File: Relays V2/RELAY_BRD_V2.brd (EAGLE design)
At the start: 43.9 x 48 mm, 20 parts, among them Q1 MMBT2222A, U1 ACS712-30A

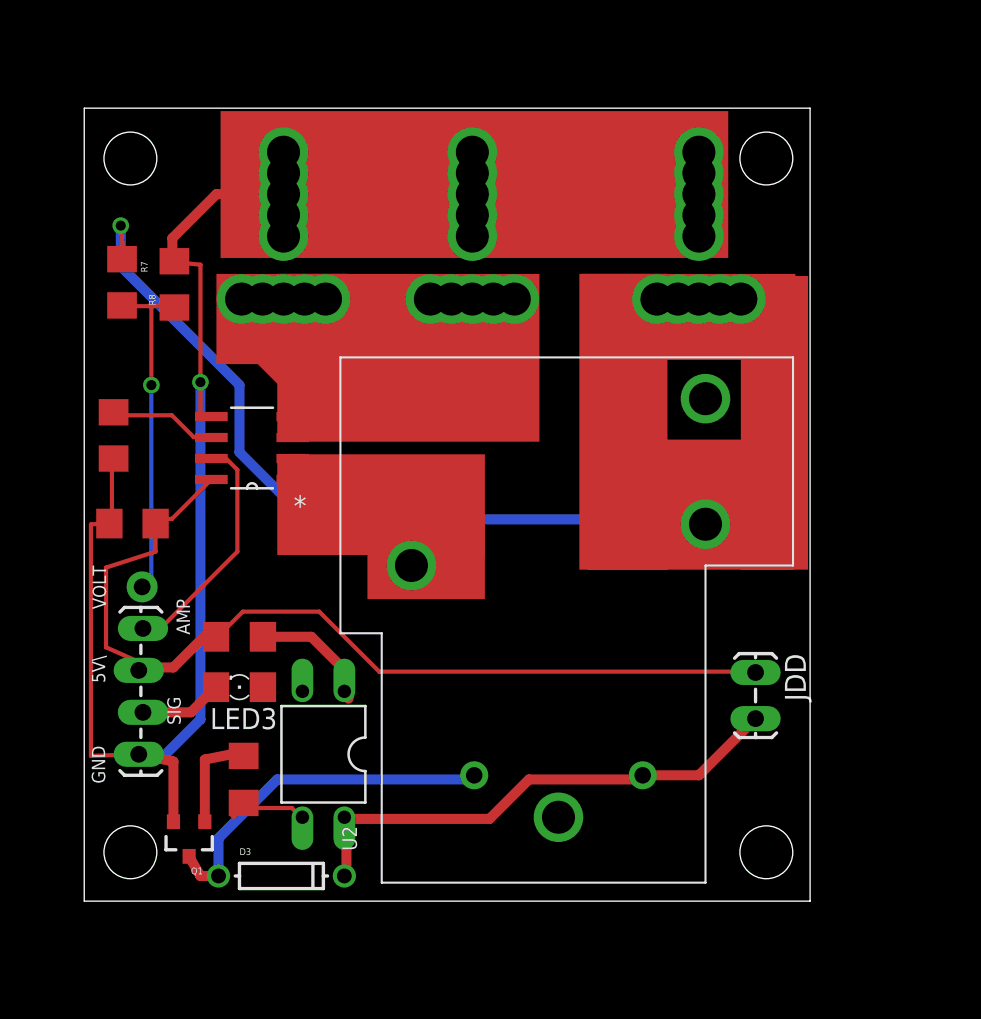
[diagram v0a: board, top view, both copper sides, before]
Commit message: added relays v2
added the new relays we will be using this year for robosub
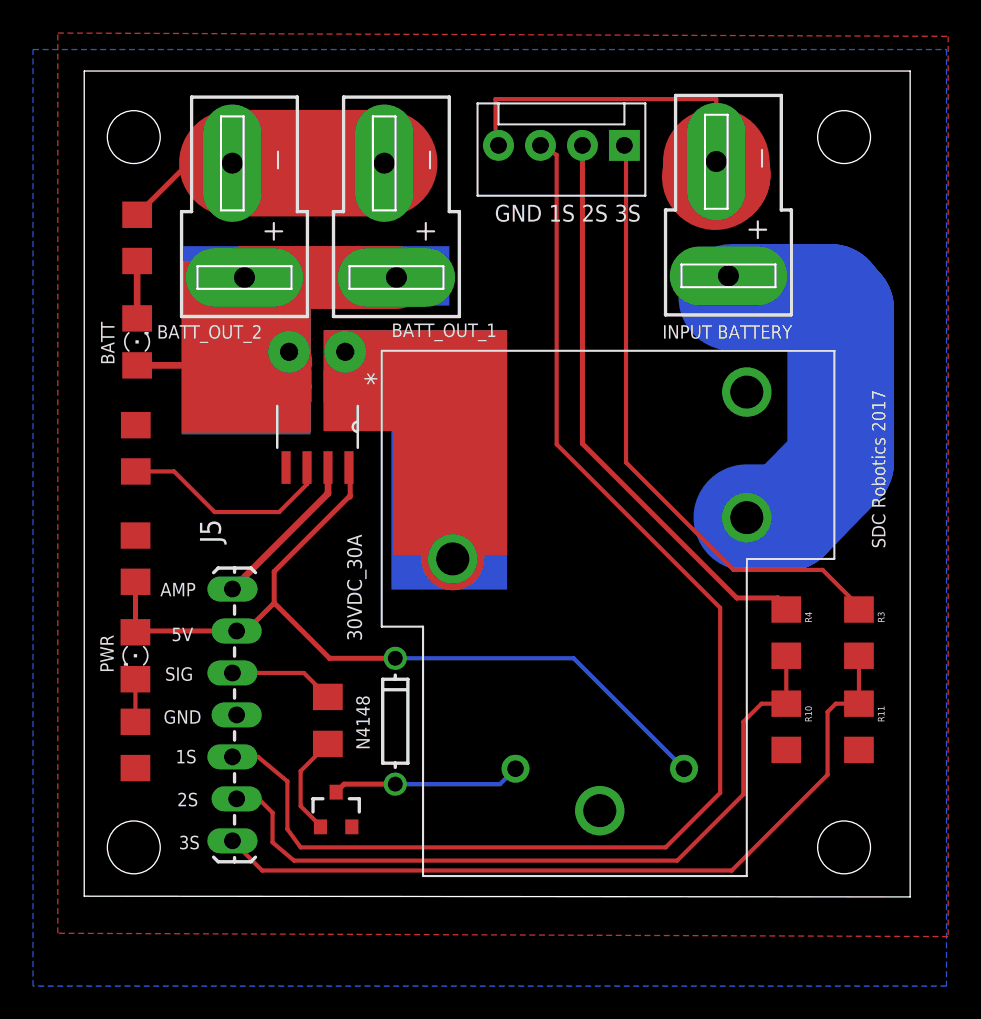
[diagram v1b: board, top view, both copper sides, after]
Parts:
- removed 11.1V_DEAN_CONNECTOR, J2, J6, J7: (no value), SparkFun-Connectors:1X01NS-KIT
- removed J9: (no value), SparkFun-Connectors:1X04_LOCK_LONGPADS
- removed JDD: (no value), SparkFun-Connectors:1X02_LOCK_LONGPADS
- removed LED3: (no value), eagle-ltspice:LED_1206
- removed OK3: PC817, optocoupler:DIL04
- removed R7: 300k, SparkFun-Passives:1206
- removed R8: 100k, SparkFun-Passives:1206
- removed U2: (no value), Grove ®C SPDT Relay(30A) v1.0:6P-19.8H
- added 30VDC_30A: (no value), Grove ®C SPDT Relay(30A) v1.0:6P-19.8H
- added BATT, PWR: (no value), eagle-ltspice:LED_1206
- added J1, J4, J8: BATTERY_CONNDEANS, SparkFun-Connectors:DEANS
- added R1: 1k, SparkFun-Resistors:1206
- added R10, R11: 100K, SparkFun-Resistors:1206
- added R2: 330, SparkFun-Resistors:1206
- added R3: 330K, SparkFun-Resistors:1206
- D3: value (none) -> N4148
- J3: device SparkFun-Connectors:1X01NS-KIT -> SparkFun-Connectors:MOLEX-1X4
- J5: device SparkFun-Connectors:1X01NS-KIT -> SparkFun-Connectors:1X07_LOCK_LONGPADS
- R4: value 1K -> 270K; device eagle-ltspice:R1206 -> SparkFun-Resistors:1206
- moved J5 48.0 mm to (9.10, 3.40), turned to 90 degrees
- moved R4 33.1 mm to (42.5, 16.0), turned to 270 degrees
- moved J3 15.0 mm to (32.7, 45.5), turned to 180 degrees
- moved D3 11.6 mm to (18.8, 10.6), turned to 90 degrees
- moved Q1 9.06 mm to (15.2, 5.24), turned to 0 degrees
- moved R6 6.23 mm to (14.7, 10.7), turned to 90 degrees
- moved U1 4.16 mm to (14.1, 28.5), turned to 270 degrees
- moved C2 2.14 mm to (3.11, 20.5), turned to 90 degrees
- moved C1 1.55 mm to (3.12, 27.2), turned to 90 degrees
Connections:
- removed net VOLTAGE_DIVIDER_5V: J6.1, R7.2, R8.1
- new net CURRENT_SENSE: J5.7, U1.7
- new net N$84: J5.2, R10.1, R4.2
- new net N$85: J5.1, R11.1, R3.2
- net 11.1V_BATTERY: now also 30VDC_30A.6, J1.+; no longer 11.1V_DEAN_CONNECTOR.1, R7.1, U2.6
- net 5V: now also 30VDC_30A.1, D3.C, J5.6, PWR.A; no longer J9.2, JDD.1, R4.2
- net GND: now also J1.-, J3.4, J4.-, J5.4, J8.-, R1.2, R10.2, R11.2, R2.2; no longer J2.1, J5.1, J7.1, J9.4, R8.2
- net N$19: now also BATT.C, R1.1; no longer LED3.A, OK3.2
- net N$20: now also J5.5, R6.2; no longer OK3.1, R4.1
- net N$21: now also PWR.C, R2.1; no longer OK3.3, R6.2
- net N$23: now also 30VDC_30A.3; no longer U2.3
- net N$24: now also J3.1, R3.1; no longer D3.C, JDD.2, OK3.4, U2.1
- net N$26: now also BATT.A, J4.+, J8.+; no longer J3.1
- net N$27: now also J3.2, R4.1; no longer J9.3, LED3.C
- net N$69: now also J3.3, J5.3; no longer J9.1, U1.7
- net N$70: now also 30VDC_30A.4; no longer U2.4
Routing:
- net N$69: track 14.4 -> 78.7 mm
- net 11.1V_BATTERY: track 87.6 -> 24.7 mm, vias 1 -> 0
- net GND: track 100.7 -> 38.9 mm, vias 1 -> 0
- net N$85: track 0.00 -> 48.0 mm
- net N$84: track 0.00 -> 45.2 mm
- net N$27: track 5.05 -> 34.6 mm
- net VOLTAGE_DIVIDER_5V: track 21.0 -> 0.00 mm, vias 1 -> 0
- net N$23: track 21.8 -> 11.4 mm
- net CURRENT_SENSE: track 0.00 -> 9.75 mm
- net N$26: track 22.0 -> 29.4 mm
- net N$24: track 31.1 -> 37.7 mm
- net N$68: track 6.53 -> 13.1 mm
- net N$70: track 12.9 -> 19.0 mm
- net 5V: track 57.6 -> 52.7 mm
- net N$19: track 0.00 -> 3.48 mm
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- added copper zone on layer 1, net GND
- added copper zone on layer 16, net GND
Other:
- board size 43.9 x 48 mm -> 50 x 50 mm
- board text added: "1S"
- board text added: "2S"
- board text added: "3S"
- board text added: "5V"
- board text added: "BATT_OUT_1"
- board text added: "BATT_OUT_2"
- board text added: "GND 1S 2S 3S"
- board text added: "INPUT BATTERY"
- board text added: "SDC Robotics 2017"
- board text removed: "5V\"
- board text removed: "VOLT"
